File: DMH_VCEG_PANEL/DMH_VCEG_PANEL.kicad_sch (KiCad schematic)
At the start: 5 parts, among them J0 Panel_GND_Solder_Wire_Pad

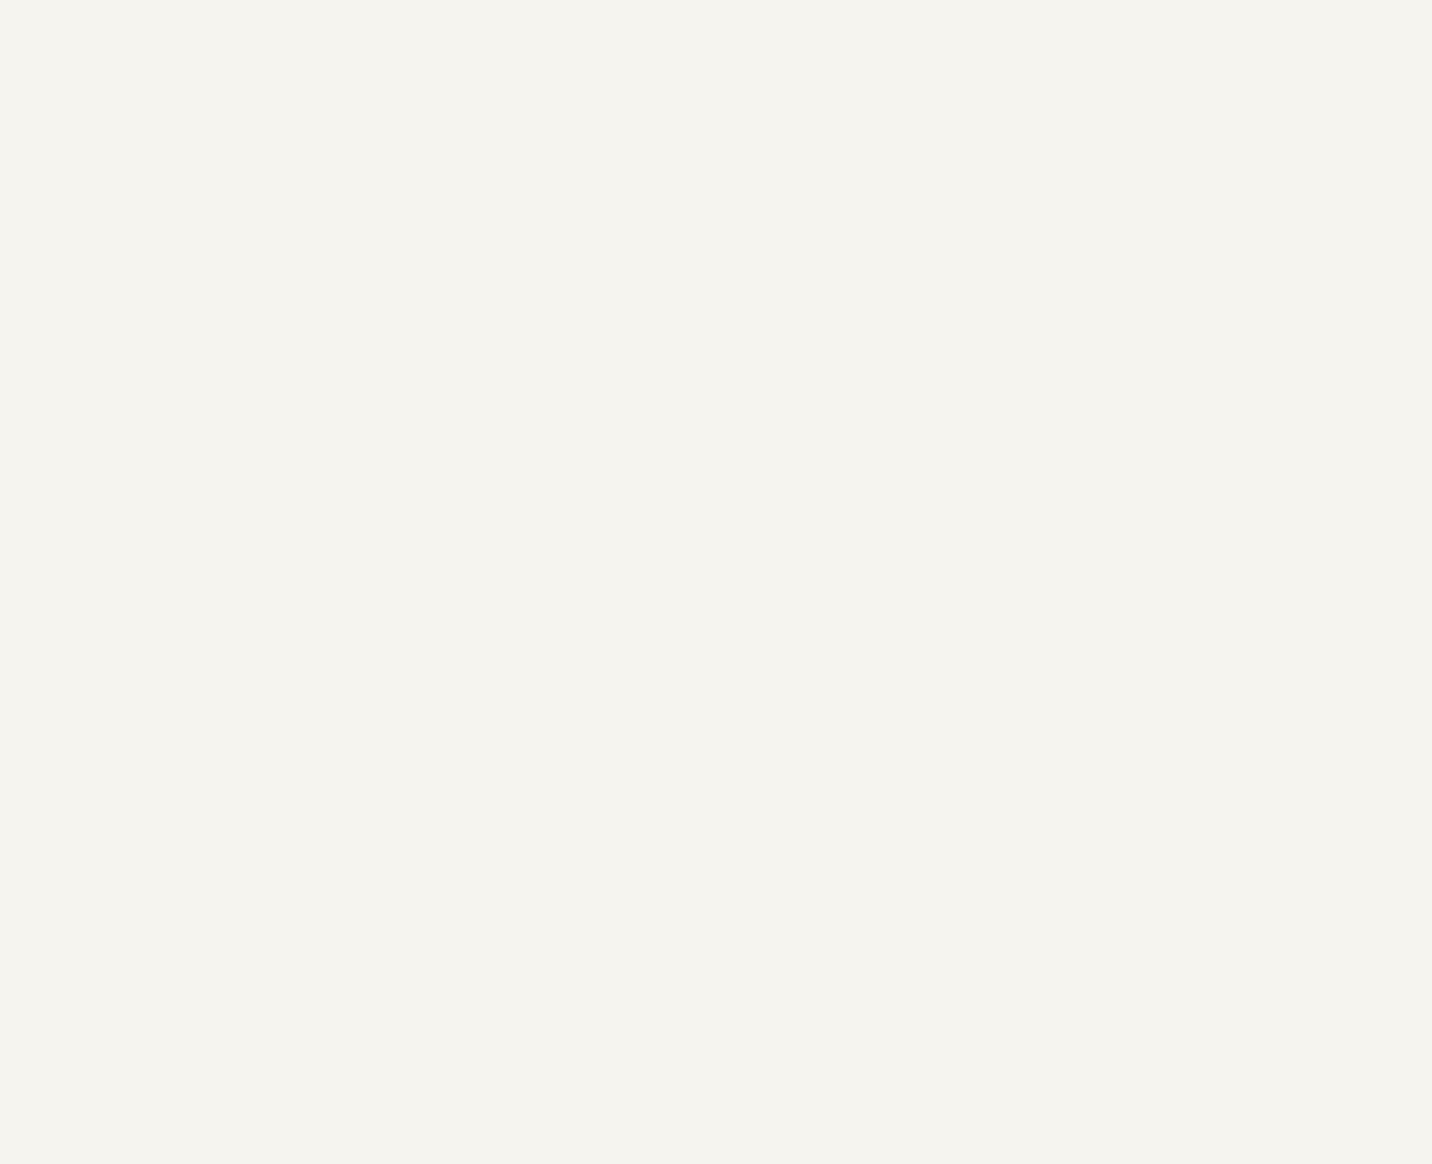
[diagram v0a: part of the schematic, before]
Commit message: Added hole symbols to Panel
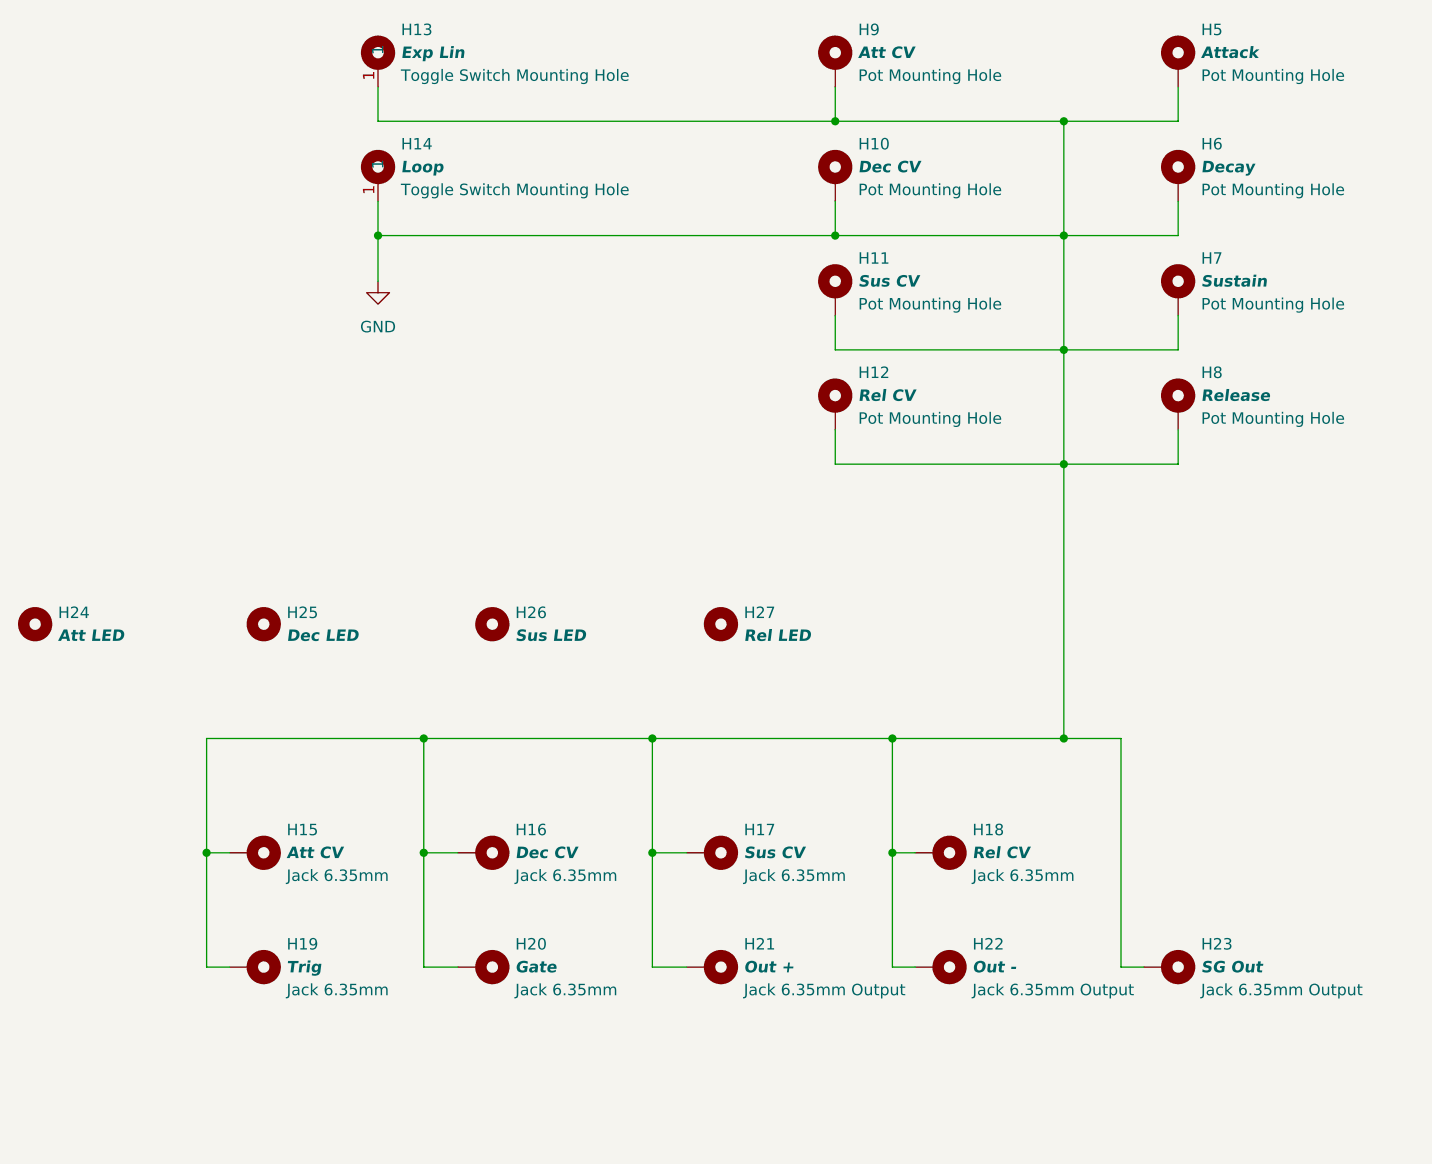
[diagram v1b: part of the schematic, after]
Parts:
- added H10: Dec CV, SynthStuff:Pot_Cutout_Tiny_attv_P110KH1, symbol SynthStuff:MountingHole_Pot
- added H11: Sus CV, SynthStuff:Pot_Cutout_Tiny_attv_P110KH1, symbol SynthStuff:MountingHole_Pot
- added H12: Rel CV, SynthStuff:Pot_Cutout_Tiny_attv_P110KH1, symbol SynthStuff:MountingHole_Pot
- added H13: Exp Lin, SynthStuff:Toggle_Switch_TE_Cutout, symbol SynthStuff:MountingHole_ToggleSwitch
- added H14: Loop, SynthStuff:Toggle_Switch_TE_Cutout, symbol SynthStuff:MountingHole_ToggleSwitch
- added H15: Att CV, SynthStuff:Jack_6.35mm_Cutout_v3, symbol SynthStuff:MountingHole_Jack6.35mm_v2
- added H16: Dec CV, SynthStuff:Jack_6.35mm_Cutout_v3, symbol SynthStuff:MountingHole_Jack6.35mm_v2
- added H17: Sus CV, SynthStuff:Jack_6.35mm_Cutout_v3, symbol SynthStuff:MountingHole_Jack6.35mm_v2
- added H18: Rel CV, SynthStuff:Jack_6.35mm_Cutout_v3, symbol SynthStuff:MountingHole_Jack6.35mm_v2
- added H19: Trig, SynthStuff:Jack_6.35mm_Cutout_v3, symbol SynthStuff:MountingHole_Jack6.35mm_v2
- added H20: Gate, SynthStuff:Jack_6.35mm_Cutout_v3, symbol SynthStuff:MountingHole_Jack6.35mm_v2
- added H21: Out +, SynthStuff:Jack_6.35mm_Cutout_Output_v6, symbol SynthStuff:MountingHole_Jack6.35mm_Output_v2
- added H22: Out -, SynthStuff:Jack_6.35mm_Cutout_Output_v6, symbol SynthStuff:MountingHole_Jack6.35mm_Output_v2
- added H23: SG Out, SynthStuff:Jack_6.35mm_Cutout_Output_v6, symbol SynthStuff:MountingHole_Jack6.35mm_Output_v2
- added H24: Att LED, SynthStuff:MountingHole_LED_3mm, symbol Mechanical:MountingHole
- added H25: Dec LED, SynthStuff:MountingHole_LED_3mm, symbol Mechanical:MountingHole
- added H26: Sus LED, SynthStuff:MountingHole_LED_3mm, symbol Mechanical:MountingHole
- added H27: Rel LED, SynthStuff:MountingHole_LED_3mm, symbol Mechanical:MountingHole
- added H5: Attack, SynthStuff:Pot_Cutout_Medium_v2, symbol SynthStuff:MountingHole_Pot
- added H6: Decay, SynthStuff:Pot_Cutout_Medium_v2, symbol SynthStuff:MountingHole_Pot
- added H7: Sustain, SynthStuff:Pot_Cutout_Medium_v2, symbol SynthStuff:MountingHole_Pot
- added H8: Release, SynthStuff:Pot_Cutout_Medium_v2, symbol SynthStuff:MountingHole_Pot
- added H9: Att CV, SynthStuff:Pot_Cutout_Tiny_attv_P110KH1, symbol SynthStuff:MountingHole_Pot
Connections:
- net GND: now also H10.1, H11.1, H12.1, H13.1, H14.1, H15.1, H16.1, H17.1, H18.1, H19.1, H20.1, H21.1, H22.1, H23.1, H5.1, H6.1, H7.1, H8.1, H9.1

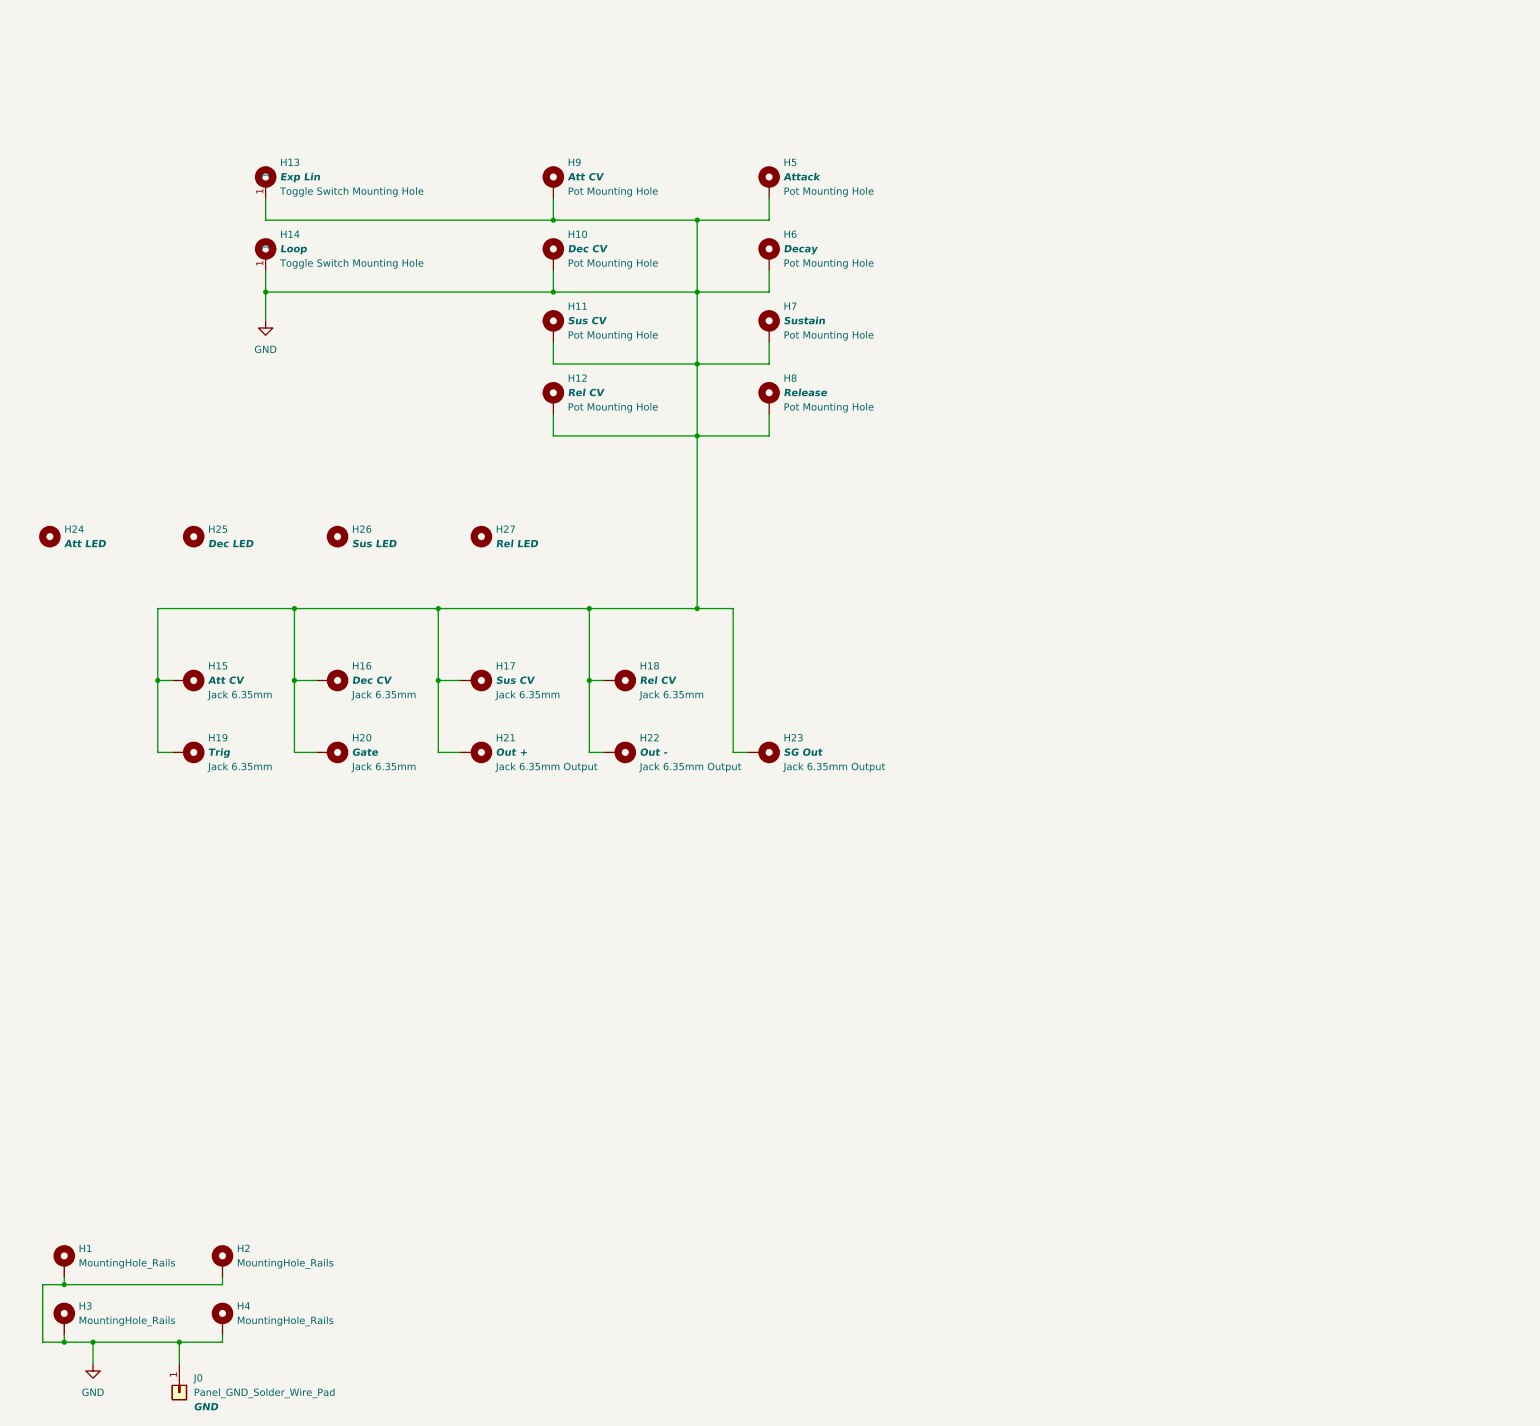
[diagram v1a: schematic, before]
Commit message: 15cm Panel design in progress
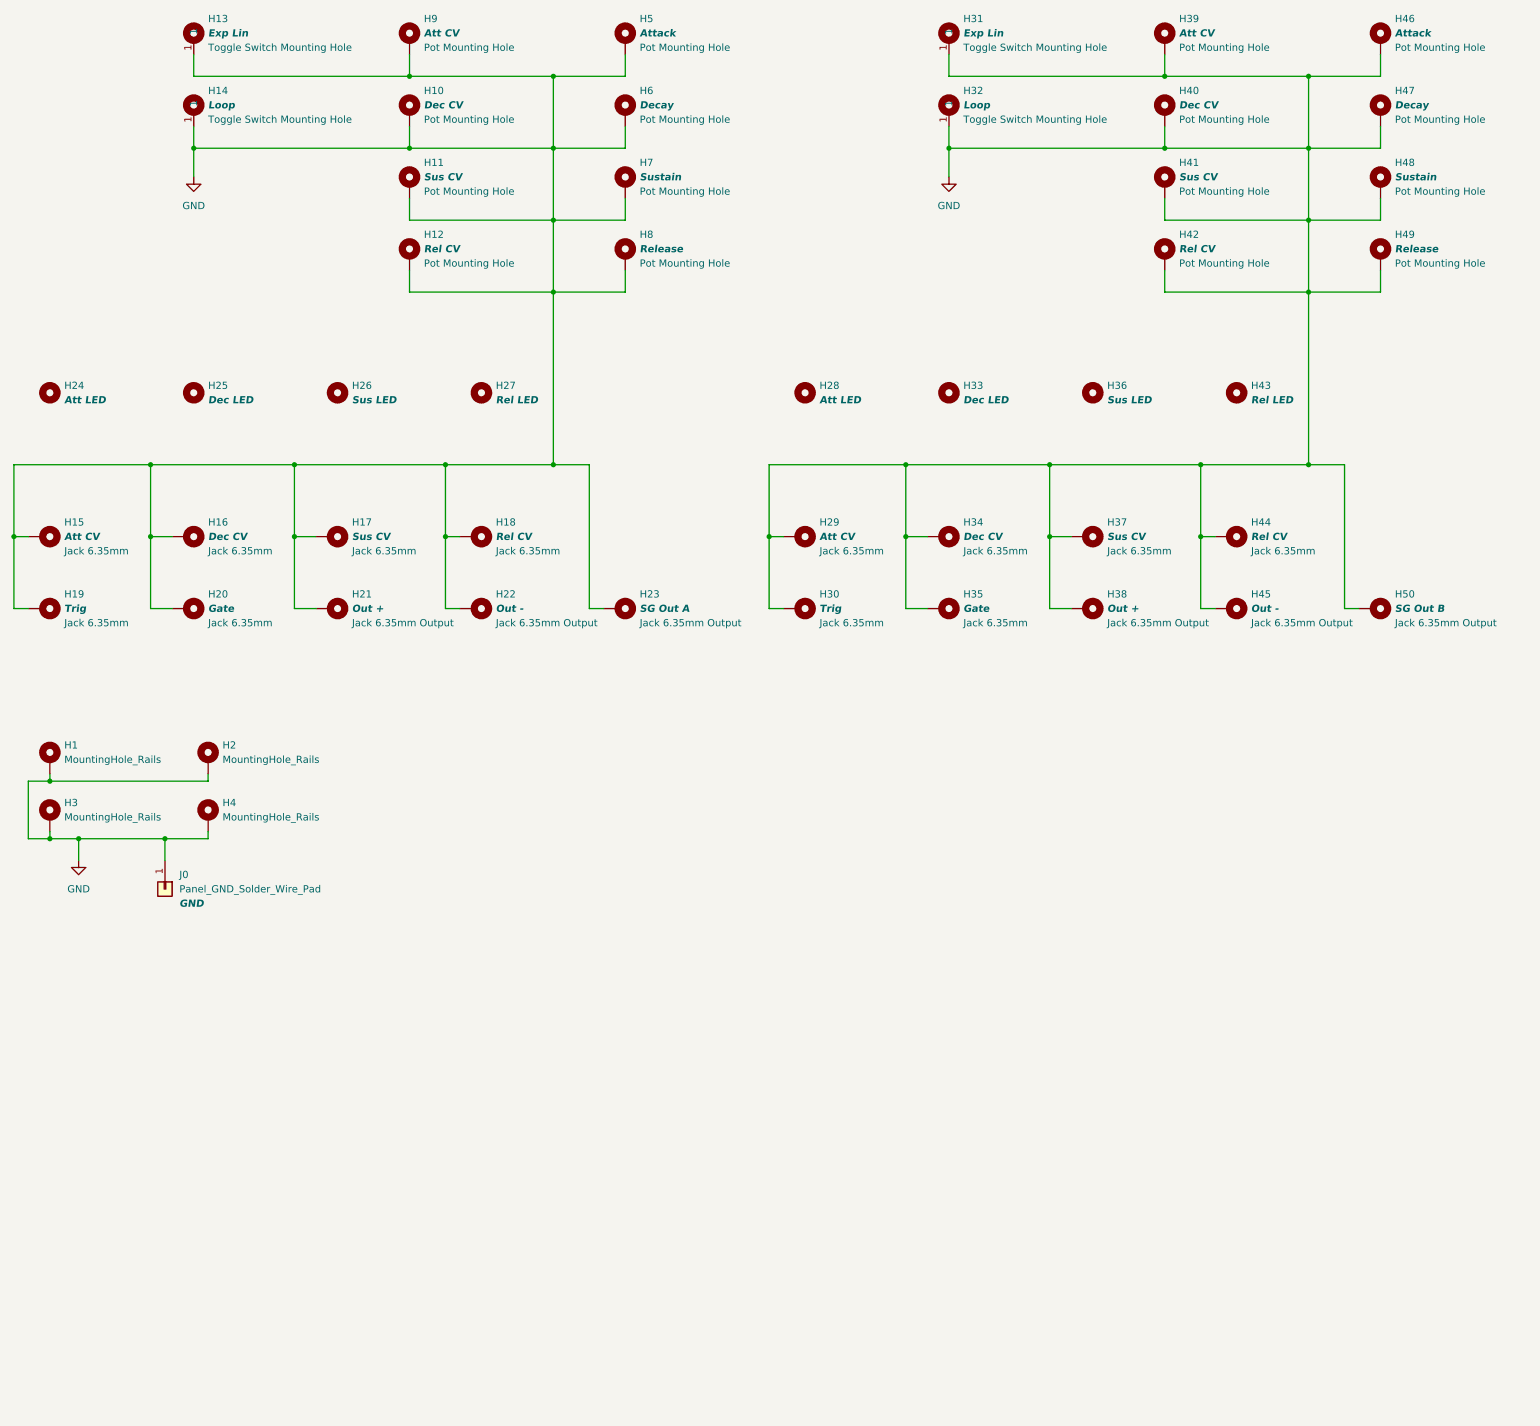
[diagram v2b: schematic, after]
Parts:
- added H28: Att LED, SynthStuff:MountingHole_LED_3mm, symbol Mechanical:MountingHole
- added H29: Att CV, SynthStuff:Jack_6.35mm_Cutout_v3, symbol SynthStuff:MountingHole_Jack6.35mm_v2
- added H30: Trig, SynthStuff:Jack_6.35mm_Cutout_v3, symbol SynthStuff:MountingHole_Jack6.35mm_v2
- added H31: Exp Lin, SynthStuff:Toggle_Switch_TE_Cutout, symbol SynthStuff:MountingHole_ToggleSwitch
- added H32: Loop, SynthStuff:Toggle_Switch_TE_Cutout, symbol SynthStuff:MountingHole_ToggleSwitch
- added H33: Dec LED, SynthStuff:MountingHole_LED_3mm, symbol Mechanical:MountingHole
- added H34: Dec CV, SynthStuff:Jack_6.35mm_Cutout_v3, symbol SynthStuff:MountingHole_Jack6.35mm_v2
- added H35: Gate, SynthStuff:Jack_6.35mm_Cutout_v3, symbol SynthStuff:MountingHole_Jack6.35mm_v2
- added H36: Sus LED, SynthStuff:MountingHole_LED_3mm, symbol Mechanical:MountingHole
- added H37: Sus CV, SynthStuff:Jack_6.35mm_Cutout_v3, symbol SynthStuff:MountingHole_Jack6.35mm_v2
- added H38: Out +, SynthStuff:Jack_6.35mm_Cutout_Output_v6, symbol SynthStuff:MountingHole_Jack6.35mm_Output_v2
- added H39: Att CV, SynthStuff:Pot_Cutout_Tiny_attv_P110KH1, symbol SynthStuff:MountingHole_Pot
- added H40: Dec CV, SynthStuff:Pot_Cutout_Tiny_attv_P110KH1, symbol SynthStuff:MountingHole_Pot
- added H41: Sus CV, SynthStuff:Pot_Cutout_Tiny_attv_P110KH1, symbol SynthStuff:MountingHole_Pot
- added H42: Rel CV, SynthStuff:Pot_Cutout_Tiny_attv_P110KH1, symbol SynthStuff:MountingHole_Pot
- added H43: Rel LED, SynthStuff:MountingHole_LED_3mm, symbol Mechanical:MountingHole
- added H44: Rel CV, SynthStuff:Jack_6.35mm_Cutout_v3, symbol SynthStuff:MountingHole_Jack6.35mm_v2
- added H45: Out -, SynthStuff:Jack_6.35mm_Cutout_Output_v6, symbol SynthStuff:MountingHole_Jack6.35mm_Output_v2
- added H46: Attack, SynthStuff:Pot_Cutout_Small, symbol SynthStuff:MountingHole_Pot
- added H47: Decay, SynthStuff:Pot_Cutout_Small, symbol SynthStuff:MountingHole_Pot
- added H48: Sustain, SynthStuff:Pot_Cutout_Small, symbol SynthStuff:MountingHole_Pot
- added H49: Release, SynthStuff:Pot_Cutout_Small, symbol SynthStuff:MountingHole_Pot
- added H50: SG Out B, SynthStuff:Jack_6.35mm_Cutout_Output_v6, symbol SynthStuff:MountingHole_Jack6.35mm_Output_v2
- H23: value SG Out -> SG Out A
- H5, H6, H7, H8: footprint SynthStuff:Pot_Cutout_Medium_v2 -> SynthStuff:Pot_Cutout_Small
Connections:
- net GND: now also H29.1, H30.1, H31.1, H32.1, H34.1, H35.1, H37.1, H38.1, H39.1, H40.1, H41.1, H42.1, H44.1, H45.1, H46.1, H47.1, H48.1, H49.1, H50.1
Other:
- title: Kosmo Format Front Panel - 10 cm -> Kosmo Format Front Panel - 15 cm
- moved on the sheet: H1, H10, H11, H12, H13, H14, H15, H16, H17, H18, H19, H2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

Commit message: Finished panel design
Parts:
- added H51, H52, H53, H54: MountingHole_Rails, SynthStuff:MountingHole_Rails, symbol SynthStuff:MountingHole_Rails
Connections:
- net GND: now also H51.1, H52.1, H53.1, H54.1

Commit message: Added amplitude CV input and pot
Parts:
- removed H22, H45: Out -, SynthStuff:Jack_6.35mm_Cutout_Output_v6, symbol SynthStuff:MountingHole_Jack6.35mm_Output_v2
- added H22, H45: Amp CV, SynthStuff:Jack_6.35mm_Cutout_v3, symbol SynthStuff:MountingHole_Jack6.35mm_v2
- added H55, H56: Amp CV, SynthStuff:Pot_Cutout_Tiny_attv_P110KH1, symbol SynthStuff:MountingHole_Pot
- H13, H31: value Exp Lin -> Exp
- H21, H38: value Out + -> Out
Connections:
- net GND: now also H22.1, H45.1, H55.1, H56.1

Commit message: Added more features
- Amp offset switch
- Re-added Out -
- Added Out R
- Rearranged positions to make everything fit
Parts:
- added H57, H58: Offset, SynthStuff:Toggle_Switch_TE_Cutout, symbol SynthStuff:MountingHole_ToggleSwitch
- added H59, H62: Out -, SynthStuff:Jack_6.35mm_Cutout_Output_v6, symbol SynthStuff:MountingHole_Jack6.35mm_Output_v2
- added H60, H61: Out R, SynthStuff:Jack_6.35mm_Cutout_Output_v6, symbol SynthStuff:MountingHole_Jack6.35mm_Output_v2
- H21, H38: value Out -> Out +
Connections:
- net GND: now also H57.1, H58.1, H59.1, H60.1, H61.1, H62.1

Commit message: Removed built in VCA
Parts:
- removed H22, H45: Amp CV, SynthStuff:Jack_6.35mm_Cutout_v3, symbol SynthStuff:MountingHole_Jack6.35mm_v2
- removed H55, H56: Amp CV, SynthStuff:Pot_Cutout_Tiny_attv_P110KH1, symbol SynthStuff:MountingHole_Pot
- removed H57, H58: Offset, SynthStuff:Toggle_Switch_TE_Cutout, symbol SynthStuff:MountingHole_ToggleSwitch
